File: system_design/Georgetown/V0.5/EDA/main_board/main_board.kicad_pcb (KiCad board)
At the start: 2 copper layers, 40.6 x 78.5 mm, 32 parts, among them J1 B3B-XH-A_LF__SN_, J2 Conn_01x02_Pin, P1 SD card socket, SW1 SW_Wuerth_450301014042, U1 HX-2S-JH10, U2 DS3231M, U3 INA219AxD, U4 BME280_module, U5 KA78M05_TO252

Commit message: PCB updated
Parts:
- added ARTS Lab: LOGO, LOGO, B.Cu at (152.0, 112.0)
- added UofSC: UofSC, LOGO, B.Cu at (152.0, 125.0)
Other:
- board text added: "Arduino Nano"
- board text added: "BME"
- board text added: "BMS"
- board text added: "DS3231"
- board text added: "Lipo"
- board text added: "SD Slot"
- board text added: "Solar"
- board text added: "Stage Height V0.5"
- board text removed: "SOL IN"
- board text removed: "V0.5"

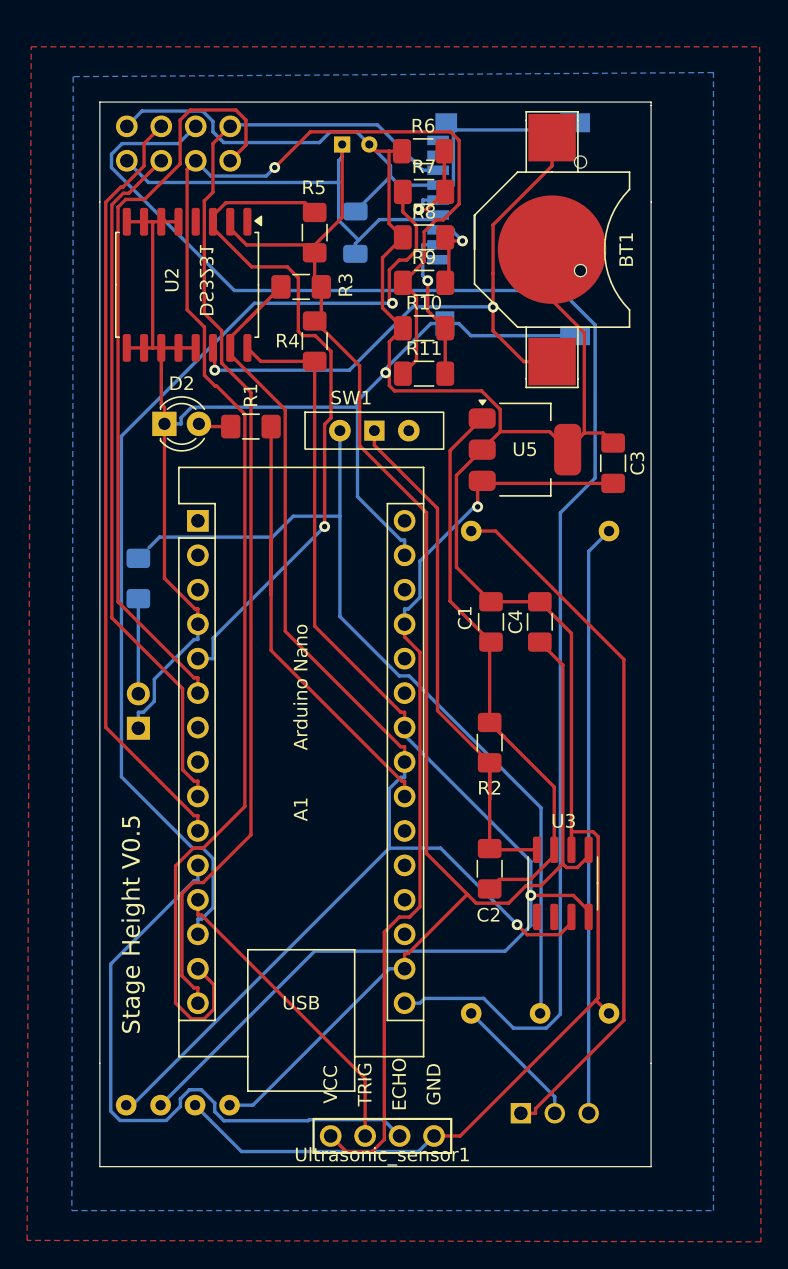
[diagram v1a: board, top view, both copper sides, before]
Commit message: PCB updated - cosmetics
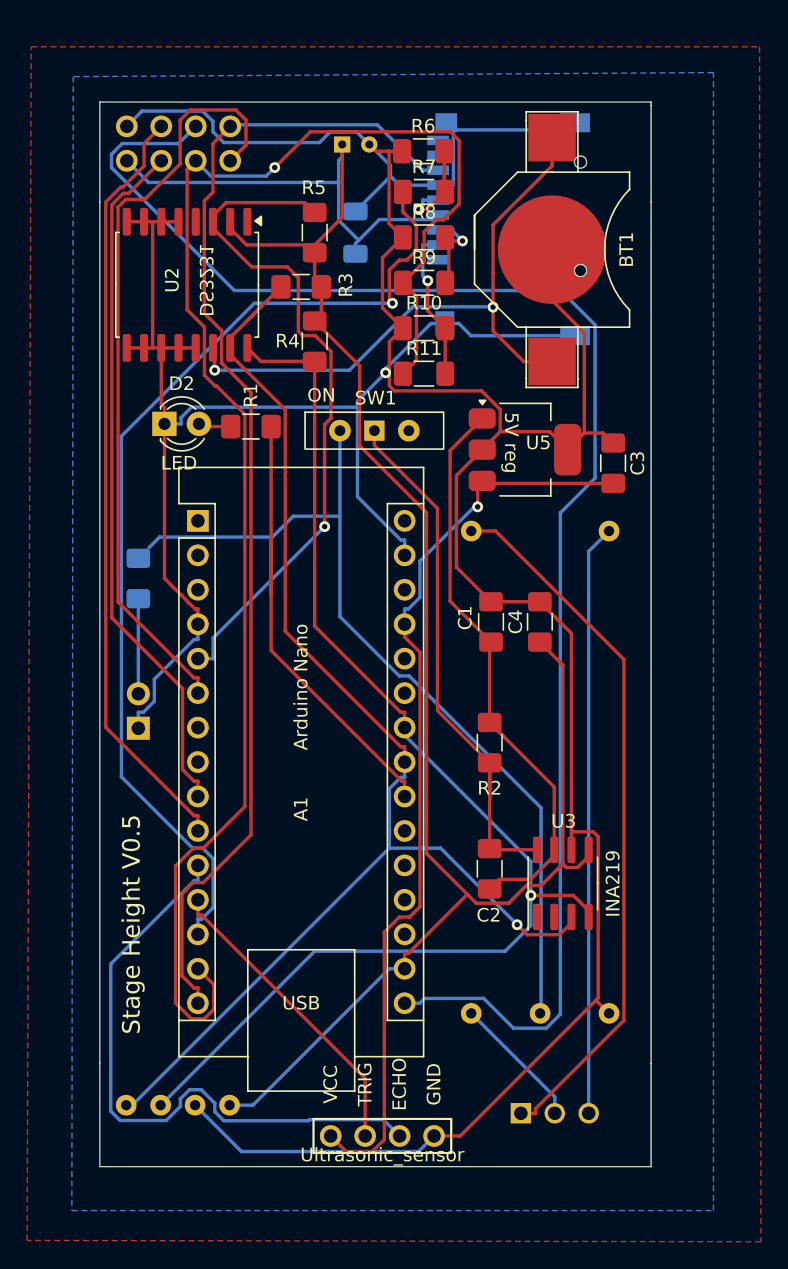
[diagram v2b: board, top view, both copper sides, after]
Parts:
- turned ARTS Lab to 0 degrees
- renumbered UofSC to USC, Ultrasonic_sensor1 to Ultrasonic_sensor
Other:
- board text added: "5V reg"
- board text added: "Amanda Sark"
- board text added: "Corinne Smith"
- board text added: "Daniel Hancock"
- board text added: "INA219"
- board text added: "LED"
- board text added: "Md A. Khan"
- board text added: "ON"
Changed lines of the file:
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@@
 	)
 	(setup
+		(stackup
+			(layer "F.SilkS"
+				(type "Top Silk Screen")
+			)
+			(layer "F.Paste"
+				(type "Top Solder Paste")
+			)
+			(layer "F.Mask"
+				(type "Top Solder Mask")
+				(thickness 0.01)
+			)
+			(layer "F.Cu"
+				(type "copper")
+				(thickness 0.035)
+			)
+			(layer "dielectric 1"
+				(type "core")
+				(thickness 1.51)
+				(material "FR4")
+				(epsilon_r 4.5)
+				(loss_tangent 0.02)
+			)
+			(layer "B.Cu"
+				(type "copper")
+				(thickness 0.035)
+			)
+			(layer "B.Mask"
+				(type "Bottom Solder Mask")
+				(thickness 0.01)
+			)
+			(layer "B.Paste"
+				(type "Bottom Solder Paste")
+			)
+			(layer "B.SilkS"
+				(type "Bottom Silk Screen")
+			)
+			(copper_finish "None")
+			(dielectric_constraints no)
+		)
 		(pad_to_mask_clearance 0.05)
 		(allow_soldermask_bridges_in_footprints no)
@@
 		(tags "CMS SOT")
 		(property "Reference" "U5"
-			(at 0 0 0)
+			(at 1 -0.5 0)
 			(layer "F.SilkS")
 			(effects
@@
 		(layer "F.Cu")
 		(at 157.99 146.33)
-		(property "Reference" "Ultrasonic_sensor1"
+		(property "Reference" "Ultrasonic_sensor"
 			(at 0 2.67 0)
 			(layer "F.SilkS")
@@
 		(tags "switch single-pole opposite-side-connection double-throw SPDT würth wurth")
 		(property "Reference" "SW1"
-			(at -1.7 -2.4 0)
+			(at 0.1 -2.4 0)
 			(layer "F.SilkS")
 			(effects
@@
 		(layer "B.Cu")
 		(at 152 125 180)
-		(property "Reference" "UofSC"
+		(property "Reference" "USC"
 			(at 0 -6.5 0)
 			(layer "B.SilkS")
@@
 	(footprint "LOGO"
 		(layer "B.Cu")
-		(at 152 112 -90)
+		(at 152 112)
 		(property "Reference" "ARTS Lab"
-			(at 4.204 -0.1 0)
+			(at 0 5 0)
 			(layer "B.SilkS")
 			(effects
@@
 		)
 		(property "Value" "LOGO"
-			(at 0.75 0 90)
+			(at 0.75 0 0)
 			(layer "B.SilkS")
 			(hide yes)
@@
 		)
 		(property "Footprint" ""
-			(at 0 0 90)
+			(at 0 0 0)
 			(layer "B.Fab")
 			(hide yes)
@@
 		)
 		(property "Datasheet" ""
-			(at 0 0 90)
+			(at 0 0 0)
 			(layer "B.Fab")
 			(hide yes)
@@
 		)
 		(property "Description" ""
-			(at 0 0 90)
+			(at 0 0 0)
 			(layer "B.Fab")
 			(hide yes)
@@
 		(at 167.43 79.48 -90)
 		(property "Reference" "P1"
-			(at 11.52 -0.07 90)
+			(at 10.52 1.43 90)
 			(layer "B.SilkS")
 			(effects
@@
 		(fp_arc
 			(start 5.168 -9.472)
-			(mid 5.659551 -9.60964)
+			(mid 5.659552 -9.609641)
 			(end 6.1679 -9.656)
 			(stroke
@@
 		)
 	)
+	(gr_text "Corinne Smith"
+		(at 171 93.5 0)
+		(layer "B.SilkS")
+		(effects
+			(font
+				(size 1.000504 1.000504)
+				(thickness 0.15)
+			)
+			(justify mirror)
+		)
+	)
+	(gr_text "Md A. Khan"
+		(at 172 98 0)
+		(layer "B.SilkS")
+		(effects
+			(font
+				(size 1.000504 1.000504)
+				(thickness 0.15)
+			)
+			(justify mirror)
+		)
+	)
+	(gr_text "Daniel Hancock"
+		(at 170.5 95 0)
+		(layer "B.SilkS")
+		(effects
+			(font
+				(size 1.000504 1.000504)
+				(thickness 0.15)
+			)
+			(justify mirror)
+		)
+	)
+	(gr_text "Amanda Sark"
+		(at 171.4 96.5 0)
+		(layer "B.SilkS")
+		(effects
+			(font
+				(size 1.000504 1.000504)
+				(thickness 0.15)
+			)
+			(justify mirror)
+		)
+	)
 	(gr_text "BMS"
-		(at 172 121.5 90)
+		(at 166 120.5 90)
 		(layer "B.SilkS")
 		(effects
@@
 	)
 	(gr_text "+"
-		(at 139 113 -90)
+		(at 139 113.5 -90)
 		(layer "B.SilkS")
 		(effects
@@
 		)
 	)
+	(gr_text "INA219"
+		(at 175 129 90)
+		(layer "F.SilkS")
+		(effects
+			(font
+				(size 1 1)
+				(thickness 0.15)
+			)
+		)
+	)
 	(gr_text "Stage Height V0.5"
 		(at 139.5 132 90)
@@
 		)
 	)
+	(gr_text "ON"
+		(at 153.5 93 0)
+		(layer "F.SilkS")
+		(effects
+			(font
+				(size 1 1)
+				(thickness 0.15)
+			)
+		)
+	)
+	(gr_text "5V reg"
+		(at 167.5 96.5 -90)
+		(layer "F.SilkS")
+		(effects
+			(font
+				(size 1 1)
+				(thickness 0.15)
+			)
+		)
+	)
 	(gr_text "Arduino Nano"
 		(at 152 114.5 90)
@@
 		)
 	)
+	(gr_text "LED"
+		(at 143 98 0)
+		(layer "F.SilkS")
+		(effects
+			(font
+				(size 1 1)
+				(thickness 0.15)
+			)
+		)
+	)

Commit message: Diode added in BOM and CAD folder cleaned
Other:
- board text added: "C"
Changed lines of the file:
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@@
 		(fp_arc
 			(start 5.168 -9.472)
-			(mid 2.945408 -8.849733)
+			(mid 2.945408 -8.849734)
 			(end 0.6469 -8.64)
 			(stroke
@@
 		(fp_arc
 			(start 5.168 -9.472)
-			(mid 5.659552 -9.609641)
+			(mid 5.659552 -9.609635)
 			(end 6.1679 -9.656)
 			(stroke
@@
 		)
 	)
+	(gr_text "C"
+		(at 140 103.5 90)
+		(layer "B.SilkS")
+		(effects
+			(font
+				(size 1 1)
+				(thickness 0.15)
+			)
+			(justify mirror)
+		)
+	)

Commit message: PCB correction for v0.5
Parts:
- C1, C2, C4: value C -> 0.1uF
- C3: value C -> 22uF
- D1: footprint Diode_SMD:D_1206_3216Metric_Pad1.42x1.75mm_HandSolder -> Diode_SMD:D_1206_3216Metric
- R2: value Rs -> 0.1
- Ultrasonic_sensor1: renamed from Ultrasonic_sensor; moved to B.Cu
- moved R3 3.98 mm to (155.8, 86.2)
- moved R5 3.00 mm to (155.7, 82.3), turned to 0 degrees
- moved R4 2.97 mm to (155.8, 90.0), turned to 180 degrees
- moved C6 2.50 mm to (155.9, 78.5), turned to 0 degrees
- moved U2 1.92 mm to (145.5, 84.6)
- moved R10 1.90 mm to (162.9, 87.5)
- moved R11 1.90 mm to (162.9, 90.9)
- moved R6 1.90 mm to (162.8, 74.5)
- moved R7 1.90 mm to (162.9, 77.5)
- moved R8 1.90 mm to (162.9, 80.8)
- moved R9 1.90 mm to (162.9, 84.2)
- moved BT1 0.81 mm to (171.3, 82.1)
- moved SW1 0.71 mm to (157.3, 94.9)
- turned Ultrasonic_sensor1 to 180 degrees
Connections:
- net Net-(A1-+5V) renamed 5V
- net Net-(A1-3V3) renamed 3V3
- net Net-(A1-D12) renamed MISO
- A1 pad 10: Net-(A1-D7) -> nRF_CS
- A1 pad 13: Net-(A1-D10) -> SD_CS
- A1 pad 14: Net-(A1-D11) -> MOSI
- A1 pad 16: Net-(A1-D13) -> SCK
- A1 pad 6: Net-(A1-D3) -> unconnected-(A1-D3-Pad6)
- A1 pad 9: Net-(A1-D6) -> nRF_CE
- R11 pad 1: Net-(A1-D11) -> SD_CS
- R7 pad 1: Net-(A1-D10) -> SCK
- R9 pad 1: Net-(A1-D11) -> MOSI
- nRF24L01+1 pad 2: Net-(A1-D6) -> nRF_CS
- nRF24L01+1 pad 3: Net-(A1-D11) -> MOSI
- nRF24L01+1 pad 4: Net-(A1-D3) -> unconnected-(nRF24L01+1-IRQ-Pad4)
- nRF24L01+1 pad 6: Net-(A1-D7) -> nRF_CE
- nRF24L01+1 pad 7: Net-(A1-D13) -> SCK
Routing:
- net GND: track 288.6 -> 0.00 mm, vias 1 -> 4
- net Net-(A1-D11): track 115.4 -> 0.00 mm, vias 1 -> 0
- net Net-(A1-D13): track 113.4 -> 0.00 mm
- net MOSI: track 0.00 -> 93.1 mm, vias 0 -> 1
- net SCK: track 0.00 -> 92.8 mm
- net Net-(A1-D10): track 74.5 -> 0.00 mm, vias 1 -> 0
- net Net-(A1-D7): track 56.7 -> 0.00 mm
- net Net-(A1-D3): track 56.5 -> 0.00 mm
- net nRF_CE: track 0.00 -> 55.2 mm
- net Net-(A1-D6): track 51.4 -> 0.00 mm
- net nRF_CS: track 0.00 -> 50.7 mm
- net SD_CS: track 0.00 -> 49.4 mm, vias 0 -> 2
- net 3V3: track 153.7 -> 187.9 mm, vias 0 -> 1
- net Net-(A1-A5): track 91.7 -> 122.3 mm, vias 1 -> 0
- net Net-(A1-D8): track 45.6 -> 26.6 mm
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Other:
- board text added: "OFF"

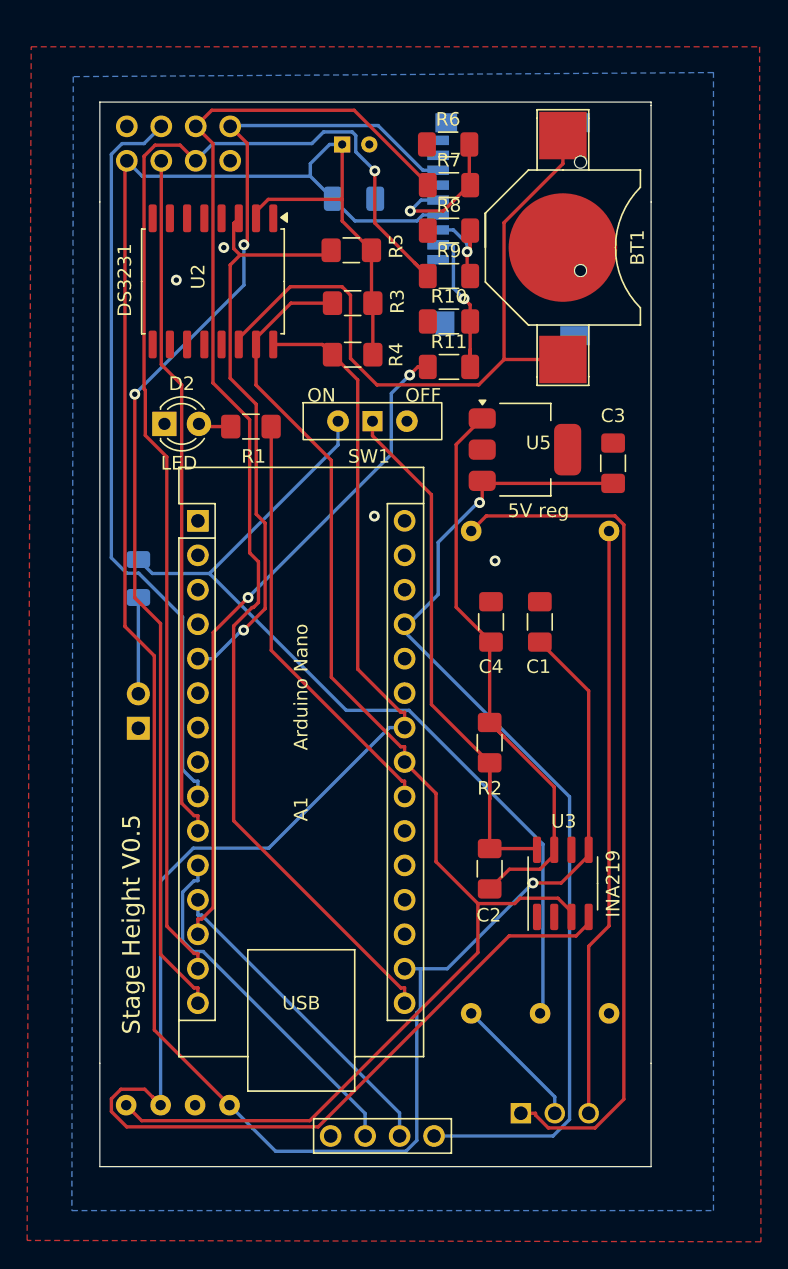
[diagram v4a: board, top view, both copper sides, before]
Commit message: PCB and chassis design changed
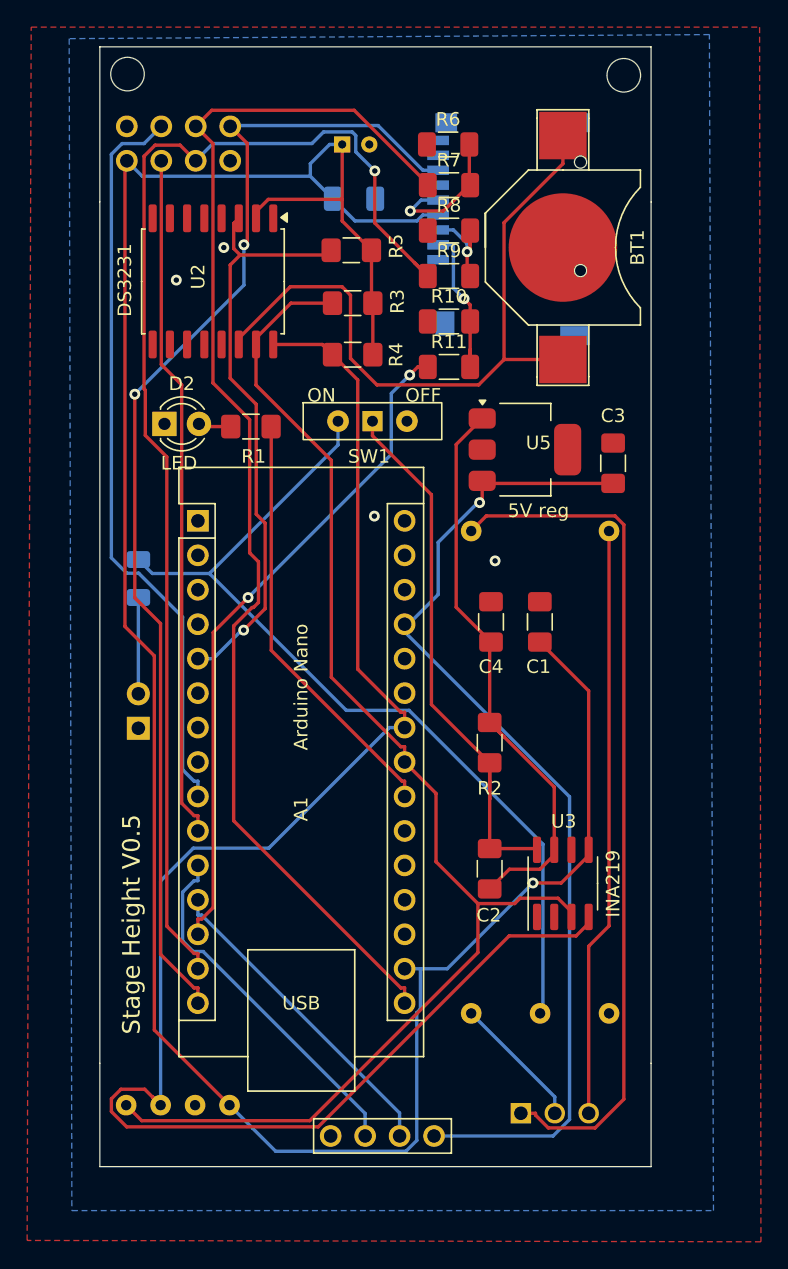
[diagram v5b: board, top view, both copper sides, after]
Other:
- board size 40.6 x 78.5 mm -> 40.6 x 82.6 mm
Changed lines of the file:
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@@
 		(tags "Through hole pin header THT 1x02 2.54mm single row")
 		(property "Reference" "J2"
-			(at 0 2.33 0)
+			(at -0.1 -6.14 0)
 			(layer "B.SilkS")
 			(effects
@@
 		(fp_arc
 			(start 5.168 -9.472)
-			(mid 5.659553 -9.609631)
+			(mid 5.659557 -9.60961)
 			(end 6.1679 -9.656)
 			(stroke
@@
 	)
 	(gr_line
-		(start 137.16 71.374)
-		(end 177.8 71.374)
+		(start 137.16 67.3)
+		(end 177.8 67.3)
 		(stroke
 			(width 0.05)
@@
 	(gr_line
 		(start 177.8 78.74)
-		(end 177.8 71.628)
+		(end 177.8 67.3)
 		(stroke
 			(width 0.05)
@@
 		(layer "Edge.Cuts")
 	)
+	(gr_circle
+		(center 139.2 69.312059)
+		(end 140.1 70.162059)
+		(stroke
+			(width 0.05)
+			(type default)
+		)
+		(fill none)
+		(layer "Edge.Cuts")
+	)
 	(gr_line
 		(start 177.8 142.24)
@@
 	)
 	(gr_line
-		(start 177.8 71.628)
-		(end 177.8 71.374)
+		(start 137.16 78.74)
+		(end 137.16 67.3)
 		(stroke
 			(width 0.05)
@@
 		(layer "Edge.Cuts")
 	)
-	(gr_line
-		(start 137.16 78.74)
-		(end 137.16 71.374)
+	(gr_circle
+		(center 175.787941 69.4)
+		(end 176.687941 70.25)
 		(stroke
 			(width 0.05)
-			(type solid)
+			(type default)
 		)
+		(fill none)
 		(layer "Edge.Cuts")
 	)
@@
 	)
 	(gr_text "Solar"
-		(at 143 114.5 90)
+		(at 141.75 122.8 0)
 		(layer "B.SilkS")
 		(effects
@@
 	)
 	(gr_text "+"
-		(at 139 113.5 -90)
+		(at 137.3 111.7 -90)
 		(layer "B.SilkS")
 		(effects
@@
 		(polygon
 			(pts
-				(xy 132.1 67.3) (xy 185.8 67.3) (xy 185.9 155.4) (xy 131.8 155.3)
+				(xy 132.1 65.85) (xy 185.8 65.85) (xy 185.9 155.4) (xy 131.8 155.3)
 			)
 		)
@@
 		(polygon
 			(pts
-				(xy 135.2 69.5) (xy 135.1 153.1) (xy 182.4 153.1) (xy 182.4 69.2)
+				(xy 134.9 66.7) (xy 135.1 153.1) (xy 182.4 153.1) (xy 182.1 66.4)
 			)
 		)
